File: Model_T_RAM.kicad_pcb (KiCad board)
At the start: 2 copper layers, 19.8 x 34.3 mm, 4 parts, among them J1 KC-85_RAM, U1 6264, U2 74HC86

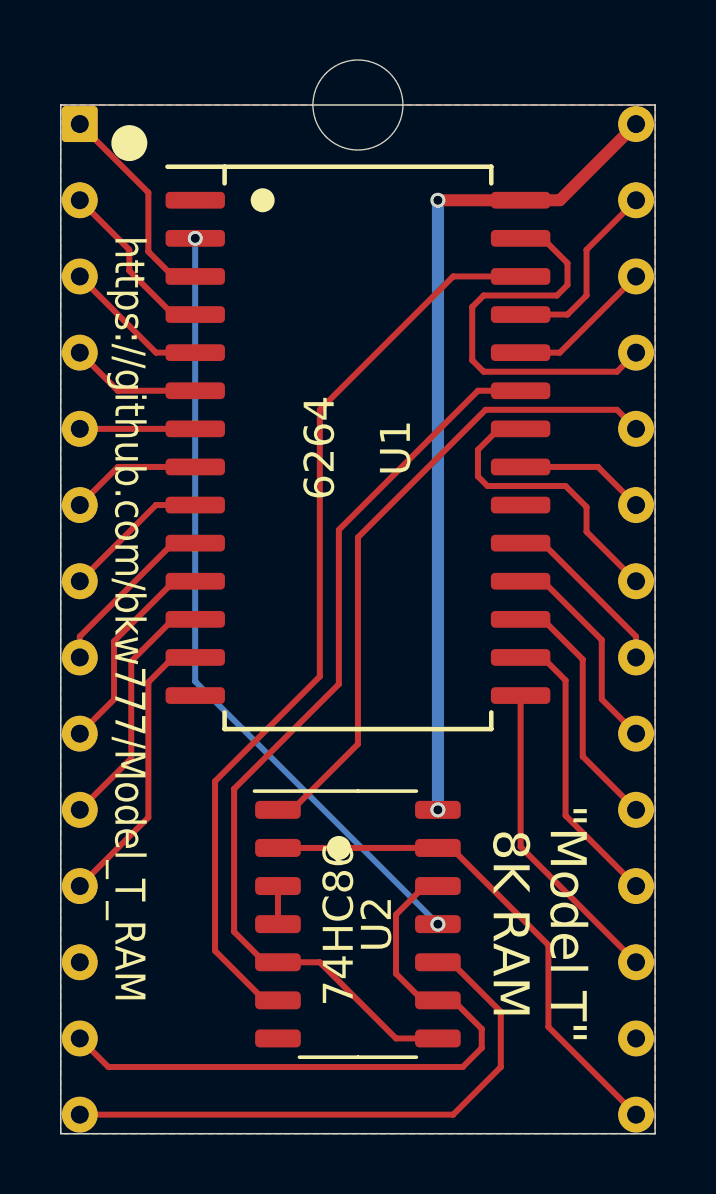
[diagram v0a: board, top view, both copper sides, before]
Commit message: v002 fewer vias
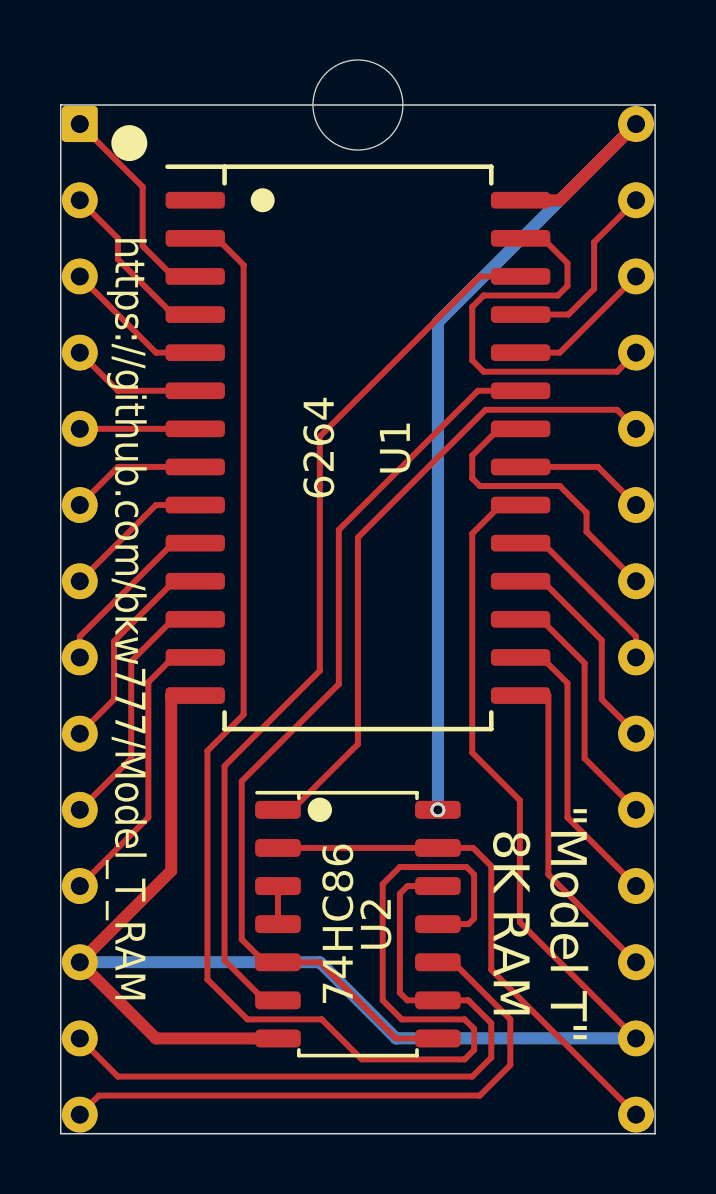
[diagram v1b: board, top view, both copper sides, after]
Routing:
- net GND: track 0.00 -> 59.3 mm
- net /A12: track 26.2 -> 50.6 mm, vias 2 -> 0
- net VCC: track 28.0 -> 30.5 mm, vias 2 -> 1
- net /~CS_A: track 22.1 -> 23.8 mm
- net /CE2: track 30.8 -> 30.0 mm
- net /AD3: track 10.5 -> 11.0 mm
- removed copper zone on B.Cu, net GND
- removed copper zone on F.Cu, net GND
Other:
- board text added: "v002"
- board text removed: "v001"

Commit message: tiny tidying
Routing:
- net /~CS_A: track 23.8 -> 23.1 mm
- net /A12: track 50.6 -> 49.9 mm

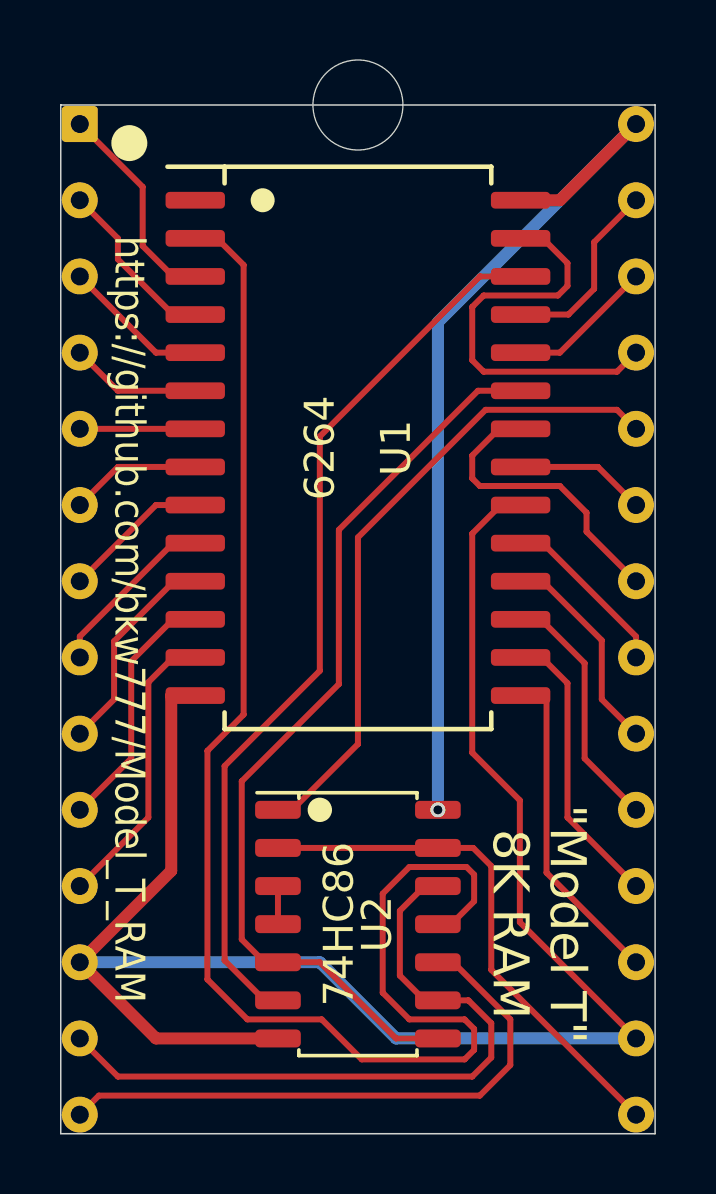
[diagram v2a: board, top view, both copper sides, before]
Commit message: switch to 74HC08
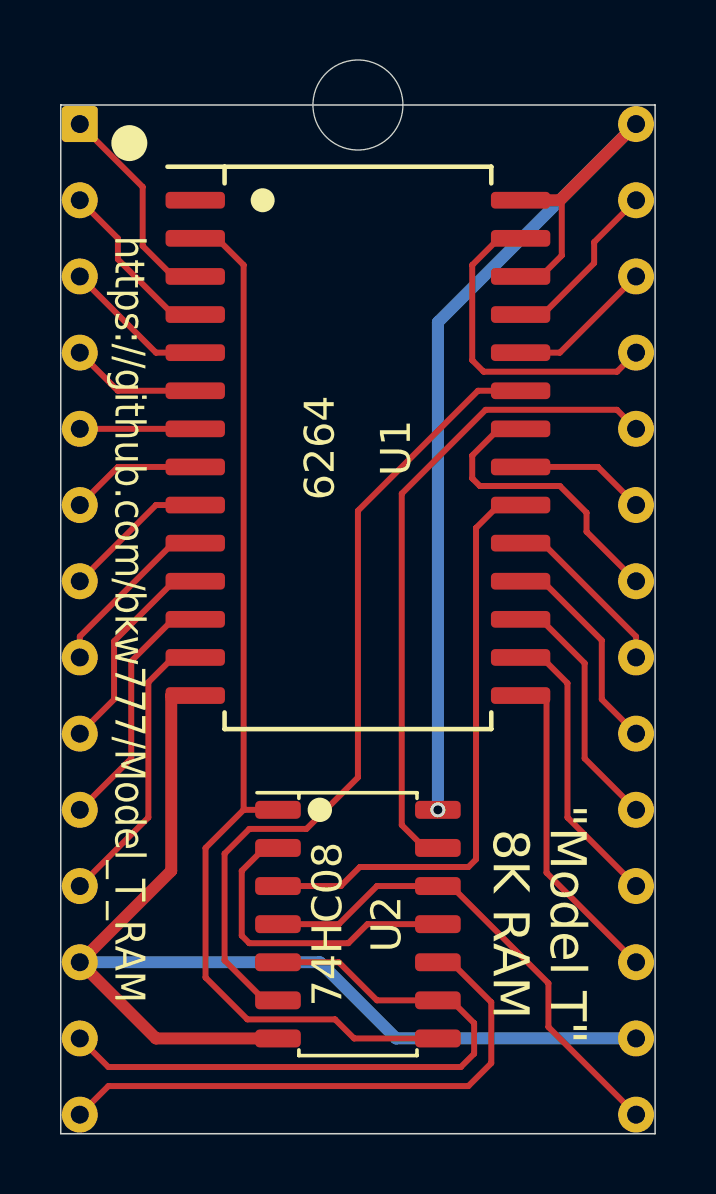
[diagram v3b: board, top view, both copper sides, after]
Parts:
- U2: value 74HC86 -> 74HC08
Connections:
- U1 pad 20: GND -> /~CE
- U1 pad 26: /CE2 -> VCC
- U2 pad 1: /~CS_D -> /A12
- U2 pad 11: /A12 -> Net-(U2-Pad11)
- U2 pad 12: /~CS_A -> /~CS_C
- U2 pad 13: /~CS_C -> /~CS_D
- U2 pad 2: /~CS_C -> Net-(U2-Pad11)
- U2 pad 3: Net-(U2-Pad3) -> /~CE
- U2 pad 4: Net-(U2-Pad3) -> /~CS_C
- U2 pad 5: /A11 -> /~CS_A
- U2 pad 6: /CE2 -> /A11
- U2 pad 8: /A11 -> /A12
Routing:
- net /CE2: track 30.0 -> 0.00 mm
- net GND: track 59.3 -> 38.2 mm
- net /~CE: track 0.00 -> 19.8 mm
- net /A12: track 49.9 -> 36.0 mm
- net Net-(U2-Pad11): track 0.00 -> 10.6 mm
- net VCC: track 30.5 -> 34.0 mm
- net /A11: track 30.9 -> 27.4 mm
- net /~WE: track 13.8 -> 11.0 mm
- net Net-(U2-Pad3): track 1.27 -> 0.00 mm
- net /~CS_C: track 17.6 -> 16.5 mm
- net /~CS_A: track 23.1 -> 22.1 mm
- net /~CS_B: track 19.8 -> 18.8 mm
- net /A8: track 6.34 -> 5.84 mm
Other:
- board text added: "v003"
- board text removed: "v002"
